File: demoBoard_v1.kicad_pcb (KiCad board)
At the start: 2 copper layers, 68 x 100 mm, 55 parts, among them P1 SPI_Header, P10 RTC_Serial, P11 WD_Header, P12 WD_1.2V_NC, P13 RTC_Aux, P14 Flash_3v3_NC, P15 WD_SENSE_3.3V_NC, P2 3x_CS_Header, P3 Power_Header, P4 LOAD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

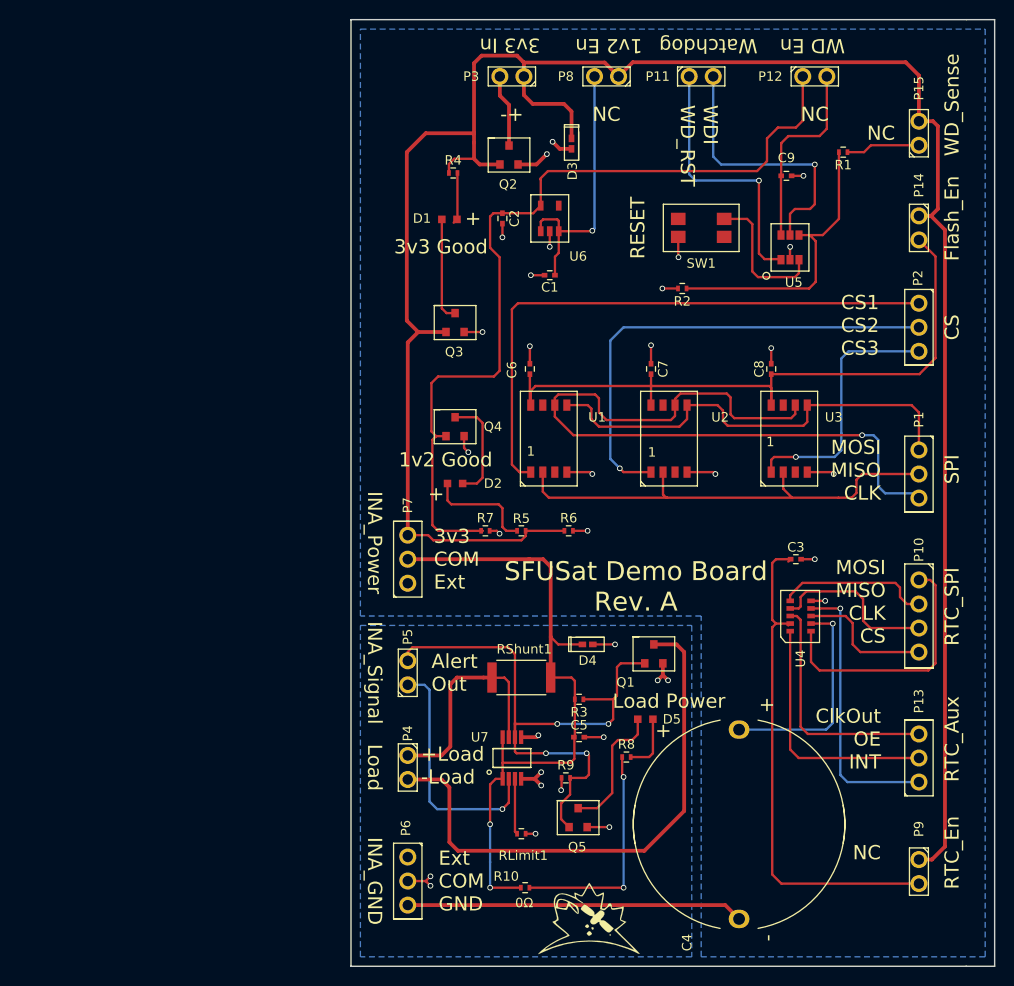
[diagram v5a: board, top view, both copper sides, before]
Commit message: Ready to be sent to board house. Last minute changed via size to be safe.
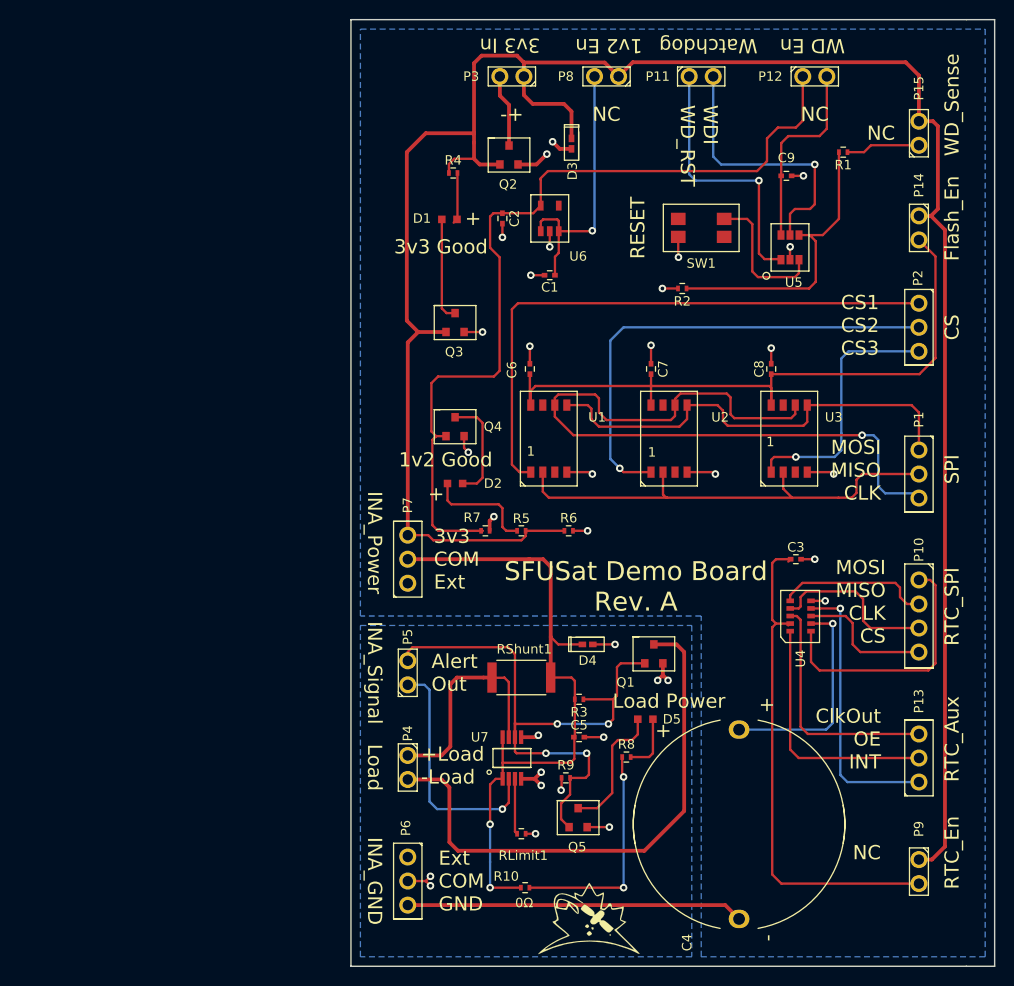
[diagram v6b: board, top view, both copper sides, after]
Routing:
- net GND: track 76.7 -> 77.3 mm
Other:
- net class Default: via_dia 0.6 -> 0.8
- rule via_min_size: 0.4 -> 0.8

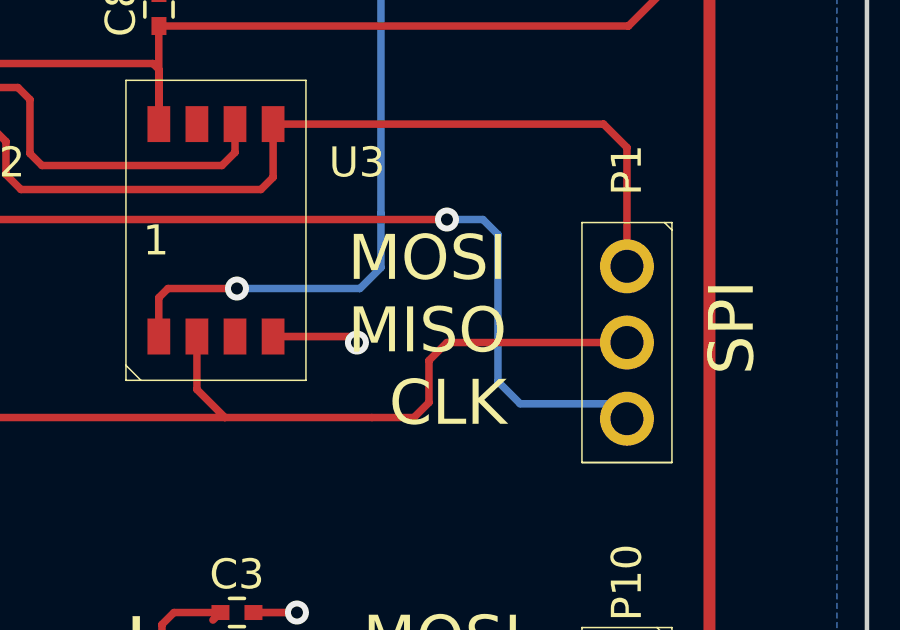
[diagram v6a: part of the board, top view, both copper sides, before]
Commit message: moved some vias to avoid a silkscreen
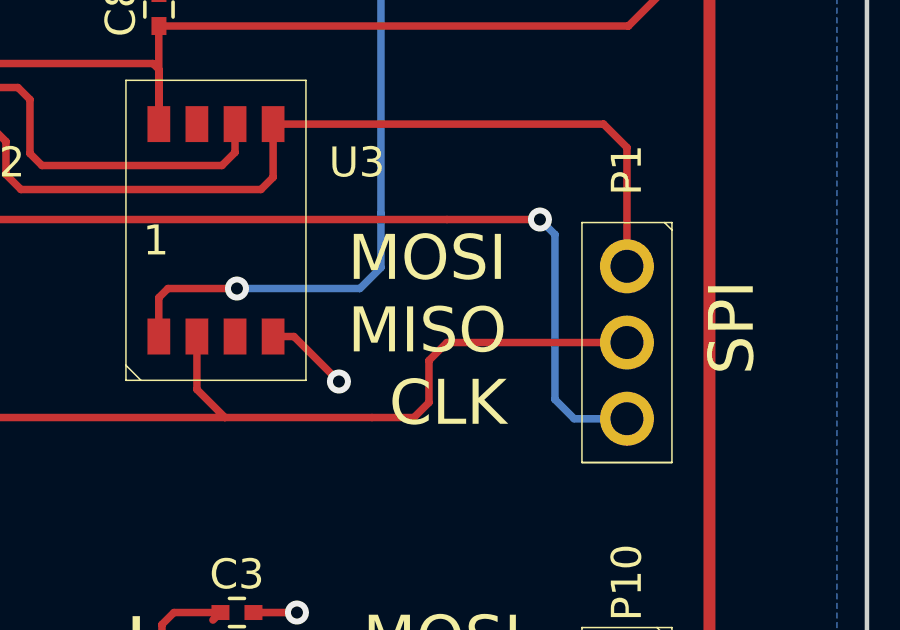
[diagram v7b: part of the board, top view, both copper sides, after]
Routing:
- net Flash_SCK: track 79.7 -> 80.2 mm
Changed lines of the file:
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@@
   )
   (setup
-    (last_trace_width 0.4)
+    (last_trace_width 0.25)
     (user_trace_width 0.254)
     (user_trace_width 0.4)
@@
     (visible_elements FFFFFF7F)
     (pcbplotparams
-      (layerselection 0x00030_80000001)
+      (layerselection 0x010f0_80000001)
       (usegerberextensions false)
       (excludeedgelayer true)
@@
       (outputformat 1)
       (mirror false)
-      (drillshape 1)
+      (drillshape 0)
       (scaleselection 1)
-      (outputdirectory ""))
+      (outputdirectory ../Desktop/Demo1_Gerber/))
   )
   (net 0 "")
@@
   (segment (start 226.95 79.65) (end 226.95 77.35) (width 0.25) (layer F.Cu) (net 1))
   (segment (start 226.55 80.05) (end 226.95 79.65) (width 0.25) (layer F.Cu) (net 1))
+  (segment (start 253.205 102.8) (end 253.9 102.8) (width 0.25) (layer F.Cu) (net 2))
+  (via (at 255.4 104.3) (size 0.8) (drill 0.4) (layers F.Cu B.Cu) (net 2))
+  (segment (start 253.9 102.8) (end 255.4 104.3) (width 0.25) (layer F.Cu) (net 2))
   (segment (start 219.65 109) (end 219.65 107.95) (width 0.4) (layer F.Cu) (net 2))
   (via (at 220.1 107.5) (size 0.8) (drill 0.4) (layers F.Cu B.Cu) (net 2))
@@
   (segment (start 252.55 112) (end 254 112) (width 0.254) (layer F.Cu) (net 2))
   (via (at 254 112) (size 0.8) (drill 0.4) (layers F.Cu B.Cu) (net 2))
-  (segment (start 253.205 102.8) (end 255.8 102.8) (width 0.254) (layer F.Cu) (net 2))
-  (via (at 256 103) (size 0.8) (drill 0.4) (layers F.Cu B.Cu) (net 2))
-  (segment (start 255.8 102.8) (end 256 103) (width 0.254) (layer F.Cu) (net 2))
   (segment (start 226 77.35) (end 226 79) (width 0.25) (layer F.Cu) (net 2))
   (via (at 226 79) (size 0.8) (drill 0.4) (layers F.Cu B.Cu) (net 2))
@@
   (segment (start 238.4 105.5) (end 251.6 105.5) (width 0.25) (layer F.Cu) (net 15))
   (segment (start 225.265 104.865) (end 225.9 105.5) (width 0.25) (layer F.Cu) (net 15))
+  (segment (start 259 98.9) (end 262.1 98.9) (width 0.25) (layer F.Cu) (net 16))
+  (segment (start 228.5 98.9) (end 259 98.9) (width 0.25) (layer F.Cu) (net 16))
+  (segment (start 226.535 96.935) (end 228.5 98.9) (width 0.25) (layer F.Cu) (net 16))
+  (segment (start 226.535 95.72) (end 226.535 96.935) (width 0.25) (layer F.Cu) (net 16))
+  (segment (start 263.24 105.54) (end 265 105.54) (width 0.25) (layer B.Cu) (net 16))
+  (segment (start 262.6 104.9) (end 263.24 105.54) (width 0.25) (layer B.Cu) (net 16))
+  (segment (start 262.6 99.4) (end 262.6 104.9) (width 0.25) (layer B.Cu) (net 16))
+  (segment (start 262.1 98.9) (end 262.6 99.4) (width 0.25) (layer B.Cu) (net 16))
+  (via (at 262.1 98.9) (size 0.8) (drill 0.4) (layers F.Cu B.Cu) (net 16))
   (segment (start 239.235 95.72) (end 239.235 95.065) (width 0.25) (layer F.Cu) (net 16))
   (segment (start 251.935 96.665) (end 251.935 95.72) (width 0.25) (layer F.Cu) (net 16))
@@
   (segment (start 226.9 94.6) (end 230.8 94.6) (width 0.25) (layer F.Cu) (net 16))
   (segment (start 226.535 94.965) (end 226.9 94.6) (width 0.25) (layer F.Cu) (net 16))
-  (segment (start 226.535 95.72) (end 226.535 96.935) (width 0.25) (layer F.Cu) (net 16))
-  (segment (start 226.535 96.935) (end 228.5 98.9) (width 0.25) (layer F.Cu) (net 16))
-  (segment (start 228.5 98.9) (end 259 98.9) (width 0.25) (layer F.Cu) (net 16))
-  (via (at 259 98.9) (size 0.8) (drill 0.4) (layers F.Cu B.Cu) (net 16))
-  (segment (start 259 98.9) (end 260.2 98.9) (width 0.25) (layer B.Cu) (net 16))
-  (segment (start 260.2 98.9) (end 260.7 99.4) (width 0.25) (layer B.Cu) (net 16))
-  (segment (start 260.7 99.4) (end 260.7 104.3) (width 0.25) (layer B.Cu) (net 16))
-  (segment (start 260.7 104.3) (end 261.44 105.04) (width 0.25) (layer B.Cu) (net 16))
-  (segment (start 261.44 105.04) (end 265 105.04) (width 0.25) (layer B.Cu) (net 16))
   (segment (start 223.995 102.8) (end 222.8 102.8) (width 0.25) (layer F.Cu) (net 17))
   (segment (start 222.64 84.96) (end 265 84.96) (width 0.25) (layer F.Cu) (net 17))

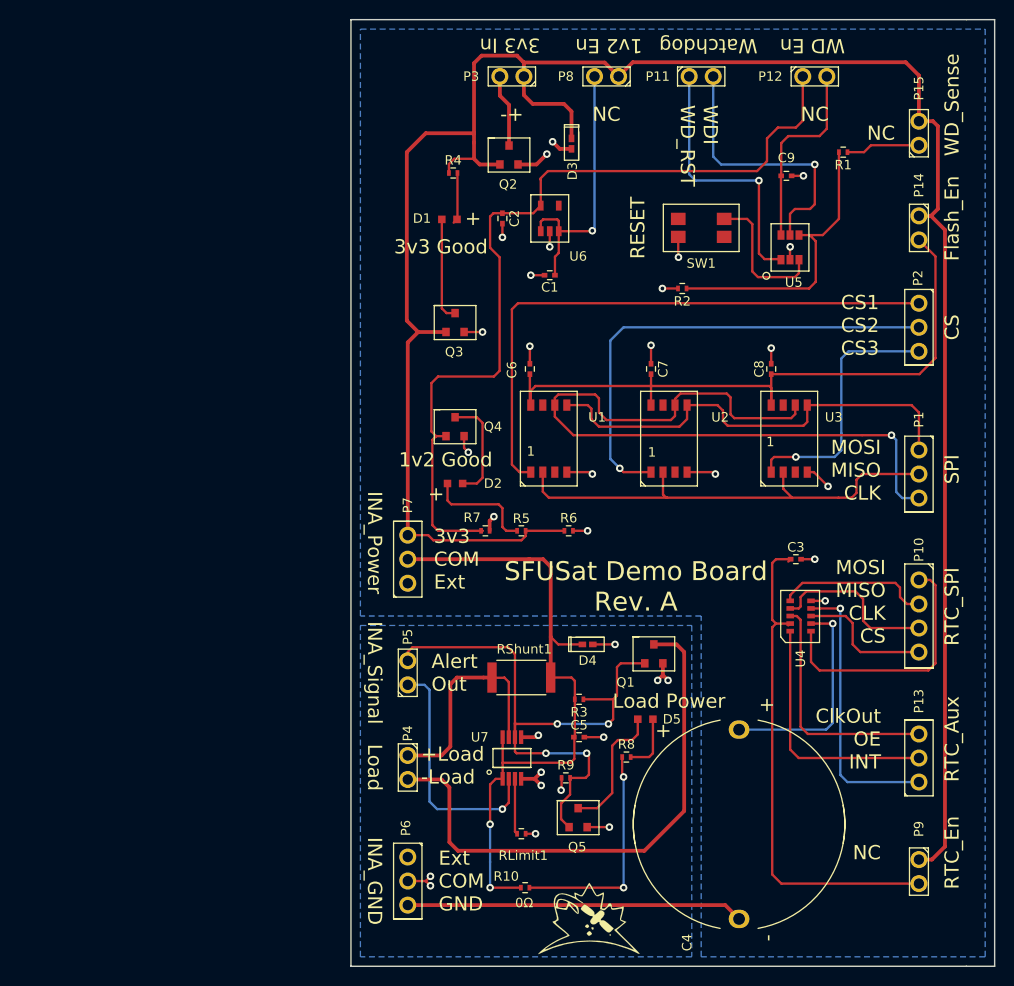
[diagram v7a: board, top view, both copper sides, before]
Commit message: Updated LED resistors to 30 ohm, turned RLimit1 into RLimit1 and RLimit2 which are values you can actually buy. Made pin header holes slightly bigger, regenerated gerbers
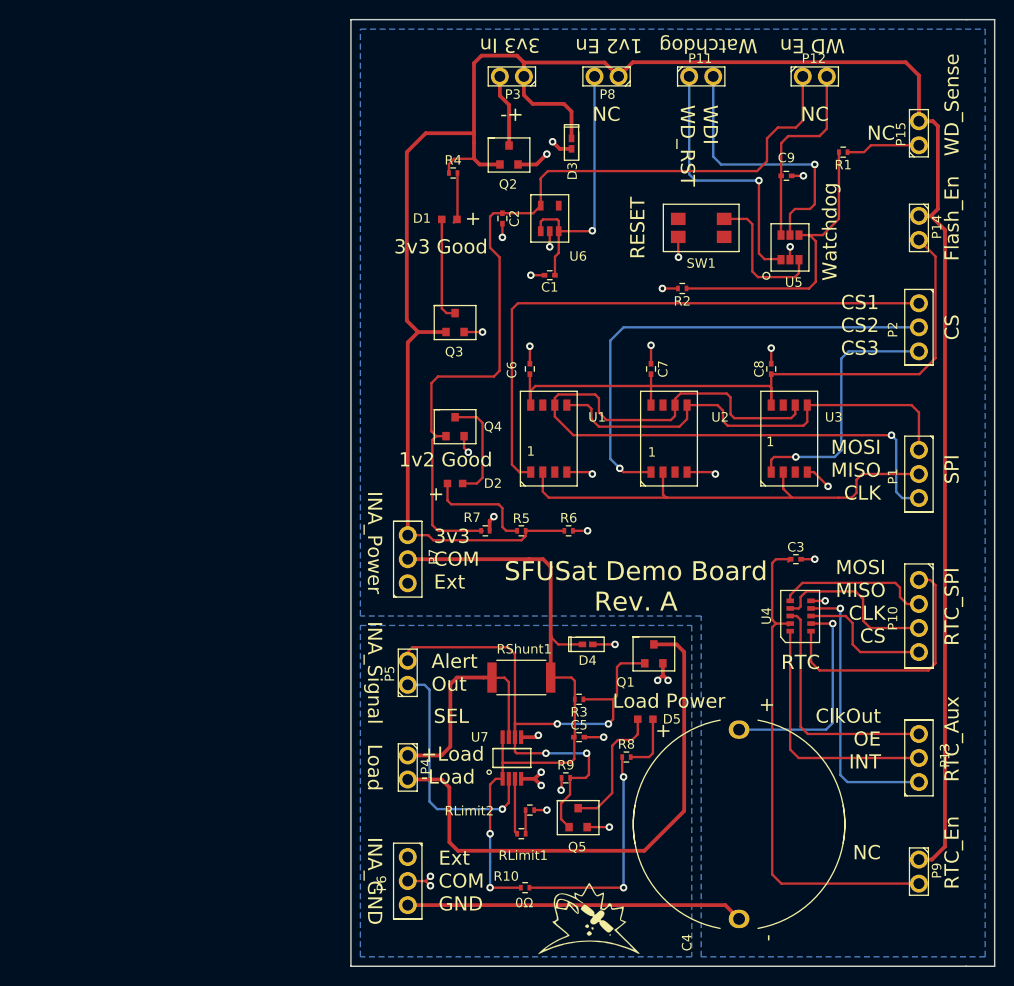
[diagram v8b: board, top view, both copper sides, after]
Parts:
- added RLimit2: 130, Resistors_SMD:R_0402, F.Cu at (223.9, 138.5)
- P1, P13, P2, P6, P7: footprint SFUSat:3x_01In_Header -> SFUSat:3x_01In_Header_v2
- P10: footprint SFUSat:4x01In_Header -> SFUSat:4x01In_Header_v2
- P11, P12, P14, P15, P3, P4, P5, P8, P9: footprint SFUSat:2x01In_Header -> SFUSat:2x01In_Header_v2
- R4, R5, R8: value 220 -> 39
- RLimit1: value 9K -> 8870
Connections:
- RLimit1 pad 2: INA_GND -> Net-(RLimit1-Pad2)
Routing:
- net Net-(RLimit1-Pad2): track 0.00 -> 2.50 mm
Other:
- board text added: "RTC"
- board text added: "SEL"
